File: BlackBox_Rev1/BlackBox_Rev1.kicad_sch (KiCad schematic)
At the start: 17 parts, among them J1 RJ45_LED_Shielded, J2 Molex_uF_SV_06, J3 Conn_02x08_Counter_Clockwise, SW1 SW_Push, SW2 SW_Push, U1 Teensy4.1_DEV-16771, U2 TSR1-2433

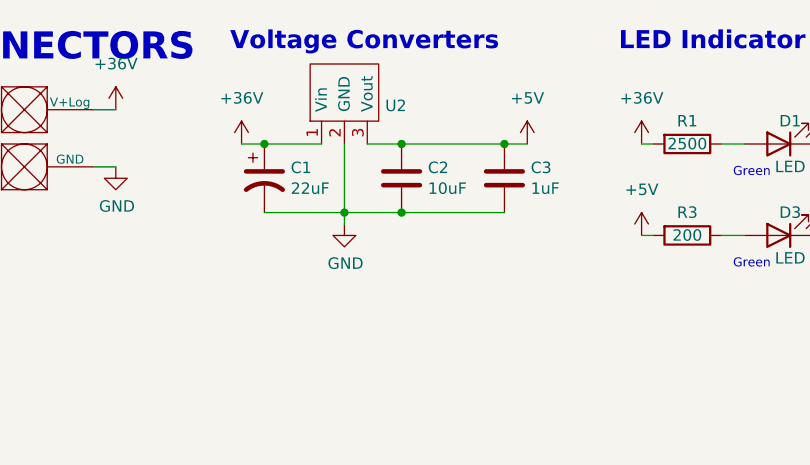
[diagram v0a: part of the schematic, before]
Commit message: change connector direction
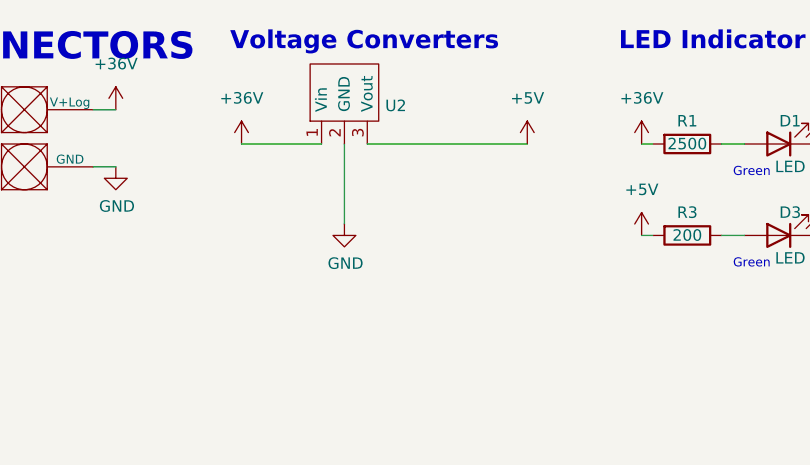
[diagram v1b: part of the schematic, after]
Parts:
- removed C1: 22uF, Capacitor_THT:CP_Radial_D5.0mm_P2.00mm, symbol BMS_2022_Rev1-rescue:CP1-Device
- removed C2: 10uF, Capacitor_SMD:C_0603_1608Metric_Pad1.08x0.95mm_HandSolder, symbol Device:C
- removed C3: 1uF, Capacitor_SMD:C_0603_1608Metric_Pad1.08x0.95mm_HandSolder, symbol Device:C
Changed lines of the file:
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@@
   (junction (at 104.14 177.8) (diameter 0) (color 0 0 0 0)
   )
-  (junction (at 67.31 34.29) (diameter 0) (color 0 0 0 0)
-  )
-  (junction (at 85.09 26.67) (diameter 0) (color 0 0 0 0)
-  )
-  (junction (at 58.42 26.67) (diameter 0) (color 0 0 0 0)
-  )
   (junction (at 66.04 189.23) (diameter 0) (color 0 0 0 0)
   )
   (junction (at 111.76 177.8) (diameter 0) (color 0 0 0 0)
-  )
-  (junction (at 73.66 34.29) (diameter 0) (color 0 0 0 0)
-  )
-  (junction (at 73.66 26.67) (diameter 0) (color 0 0 0 0)
   )
   (junction (at 104.14 166.37) (diameter 0) (color 0 0 0 0)
@@
     (stroke (width 0) (type default) (color 0 0 0 0))
   )
-  (wire (pts (xy 67.31 34.29) (xy 67.31 35.56))
-    (stroke (width 0) (type default) (color 0 0 0 0))
-  )
-  (wire (pts (xy 55.88 26.67) (xy 58.42 26.67))
-    (stroke (width 0) (type default) (color 0 0 0 0))
-  )
-  (wire (pts (xy 67.31 34.29) (xy 73.66 34.29))
+  (wire (pts (xy 67.31 26.67) (xy 67.31 35.56))
     (stroke (width 0) (type default) (color 0 0 0 0))
   )
@@
     (stroke (width 0) (type default) (color 0 0 0 0))
   )
-  (wire (pts (xy 85.09 26.67) (xy 87.63 26.67))
+  (wire (pts (xy 69.85 26.67) (xy 87.63 26.67))
     (stroke (width 0) (type default) (color 0 0 0 0))
   )
@@
     (stroke (width 0) (type default) (color 0 0 0 0))
   )
-  (wire (pts (xy 73.66 26.67) (xy 85.09 26.67))
-    (stroke (width 0) (type default) (color 0 0 0 0))
-  )
   (wire (pts (xy 156.21 152.4) (xy 158.75 152.4))
     (stroke (width 0) (type default) (color 0 0 0 0))
@@
     (stroke (width 0) (type default) (color 0 0 0 0))
   )
-  (wire (pts (xy 58.42 34.29) (xy 67.31 34.29))
-    (stroke (width 0) (type default) (color 0 0 0 0))
-  )
   (wire (pts (xy 118.11 137.16) (xy 118.11 180.34))
     (stroke (width 0) (type default) (color 0 0 0 0))
@@
     (stroke (width 0) (type default) (color 0 0 0 0))
   )
-  (wire (pts (xy 73.66 34.29) (xy 85.09 34.29))
-    (stroke (width 0) (type default) (color 0 0 0 0))
-  )
   (wire (pts (xy 104.14 160.02) (xy 104.14 166.37))
     (stroke (width 0) (type default) (color 0 0 0 0))
@@
     (stroke (width 0) (type default) (color 0 0 0 0))
   )
-  (wire (pts (xy 58.42 26.67) (xy 64.77 26.67))
+  (wire (pts (xy 55.88 26.67) (xy 64.77 26.67))
     (stroke (width 0) (type default) (color 0 0 0 0))
   )
@@
     (stroke (width 0) (type default) (color 0 0 0 0))
   )
-  (wire (pts (xy 67.31 26.67) (xy 67.31 34.29))
-    (stroke (width 0) (type default) (color 0 0 0 0))
-  )
   (wire (pts (xy 171.45 152.4) (xy 173.99 152.4))
-    (stroke (width 0) (type default) (color 0 0 0 0))
-  )
-  (wire (pts (xy 69.85 26.67) (xy 73.66 26.67))
     (stroke (width 0) (type default) (color 0 0 0 0))
   )
@@
     (pin "1")
   )
-  (symbol (lib_id "Device:C") (at 73.66 30.48 0) (unit 1)
-    (in_bom yes) (on_board yes)
-    (property "Reference" "C2" (id 0) (at 76.581 29.3116 0)
-      (effects (font (size 1.27 1.27)) (justify left))
-    )
-    (property "Value" "10uF" (id 1) (at 76.581 31.623 0)
-      (effects (font (size 1.27 1.27)) (justify left))
-    )
-    (property "Footprint" "Capacitor_SMD:C_0603_1608Metric_Pad1.08x0.95mm_HandSolder" (id 2) (at 74.6252 34.29 0)
-      (effects (font (size 1.27 1.27)) hide)
-    )
-    (property "Datasheet" "~" (id 3) (at 73.66 30.48 0)
-      (effects (font (size 1.27 1.27)) hide)
-    )
-    (pin "1")
-    (pin "2")
-  )
   (symbol (lib_id "power:+5V") (at 87.63 26.67 0) (unit 1)
     (in_bom yes) (on_board yes) (fields_autoplaced)
@@
     (pin "SH")
   )
-  (symbol (lib_id "BMS_2022_Rev1-rescue:CP1-Device") (at 58.42 30.48 0) (unit 1)
-    (in_bom yes) (on_board yes)
-    (property "Reference" "C1" (id 0) (at 61.341 29.3116 0)
-      (effects (font (size 1.27 1.27)) (justify left))
-    )
-    (property "Value" "22uF" (id 1) (at 61.341 31.623 0)
-      (effects (font (size 1.27 1.27)) (justify left))
-    )
-    (property "Footprint" "Capacitor_THT:CP_Radial_D5.0mm_P2.00mm" (id 2) (at 58.42 30.48 0)
-      (effects (font (size 1.27 1.27)) hide)
-    )
-    (property "Datasheet" "~" (id 3) (at 58.42 30.48 0)
-      (effects (font (size 1.27 1.27)) hide)
-    )
-    (pin "1")
-    (pin "2")
-  )
   (symbol (lib_id "power:GND") (at 87.63 152.4 0) (unit 1)
     (in_bom yes) (on_board yes)
@@
     (pin "1")
   )
-  (symbol (lib_id "Device:C") (at 85.09 30.48 0) (unit 1)
-    (in_bom yes) (on_board yes)
-    (property "Reference" "C3" (id 0) (at 88.011 29.3116 0)
-      (effects (font (size 1.27 1.27)) (justify left))
-    )
-    (property "Value" "1uF" (id 1) (at 88.011 31.623 0)
-      (effects (font (size 1.27 1.27)) (justify left))
-    )
-    (property "Footprint" "Capacitor_SMD:C_0603_1608Metric_Pad1.08x0.95mm_HandSolder" (id 2) (at 86.0552 34.29 0)
-      (effects (font (size 1.27 1.27)) hide)
-    )
-    (property "Datasheet" "~" (id 3) (at 85.09 30.48 0)
-      (effects (font (size 1.27 1.27)) hide)
-    )
-    (pin "1")
-    (pin "2")
-  )
   (symbol (lib_id "power:GND") (at 121.92 26.67 0) (unit 1)
     (in_bom yes) (on_board yes)
@@
       (reference "#PWR0106") (unit 1) (value "GND") (footprint "")
     )
-    (path "/c66825b9-5143-4c83-90ee-8bd89d91f6cd"
-      (reference "C1") (unit 1) (value "22uF") (footprint "Capacitor_THT:CP_Radial_D5.0mm_P2.00mm")
-    )
-    (path "/b0f91748-63da-4b62-9113-8f4f59d6fbad"
-      (reference "C2") (unit 1) (value "10uF") (footprint "Capacitor_SMD:C_0603_1608Metric_Pad1.08x0.95mm_HandSolder")
-    )
-    (path "/f1873180-95f5-41e2-bc79-a07462325bb2"
-      (reference "C3") (unit 1) (value "1uF") (footprint "Capacitor_SMD:C_0603_1608Metric_Pad1.08x0.95mm_HandSolder")
-    )
     (path "/9d9ed59e-cc22-4a1e-998b-26ca9d73f23c"

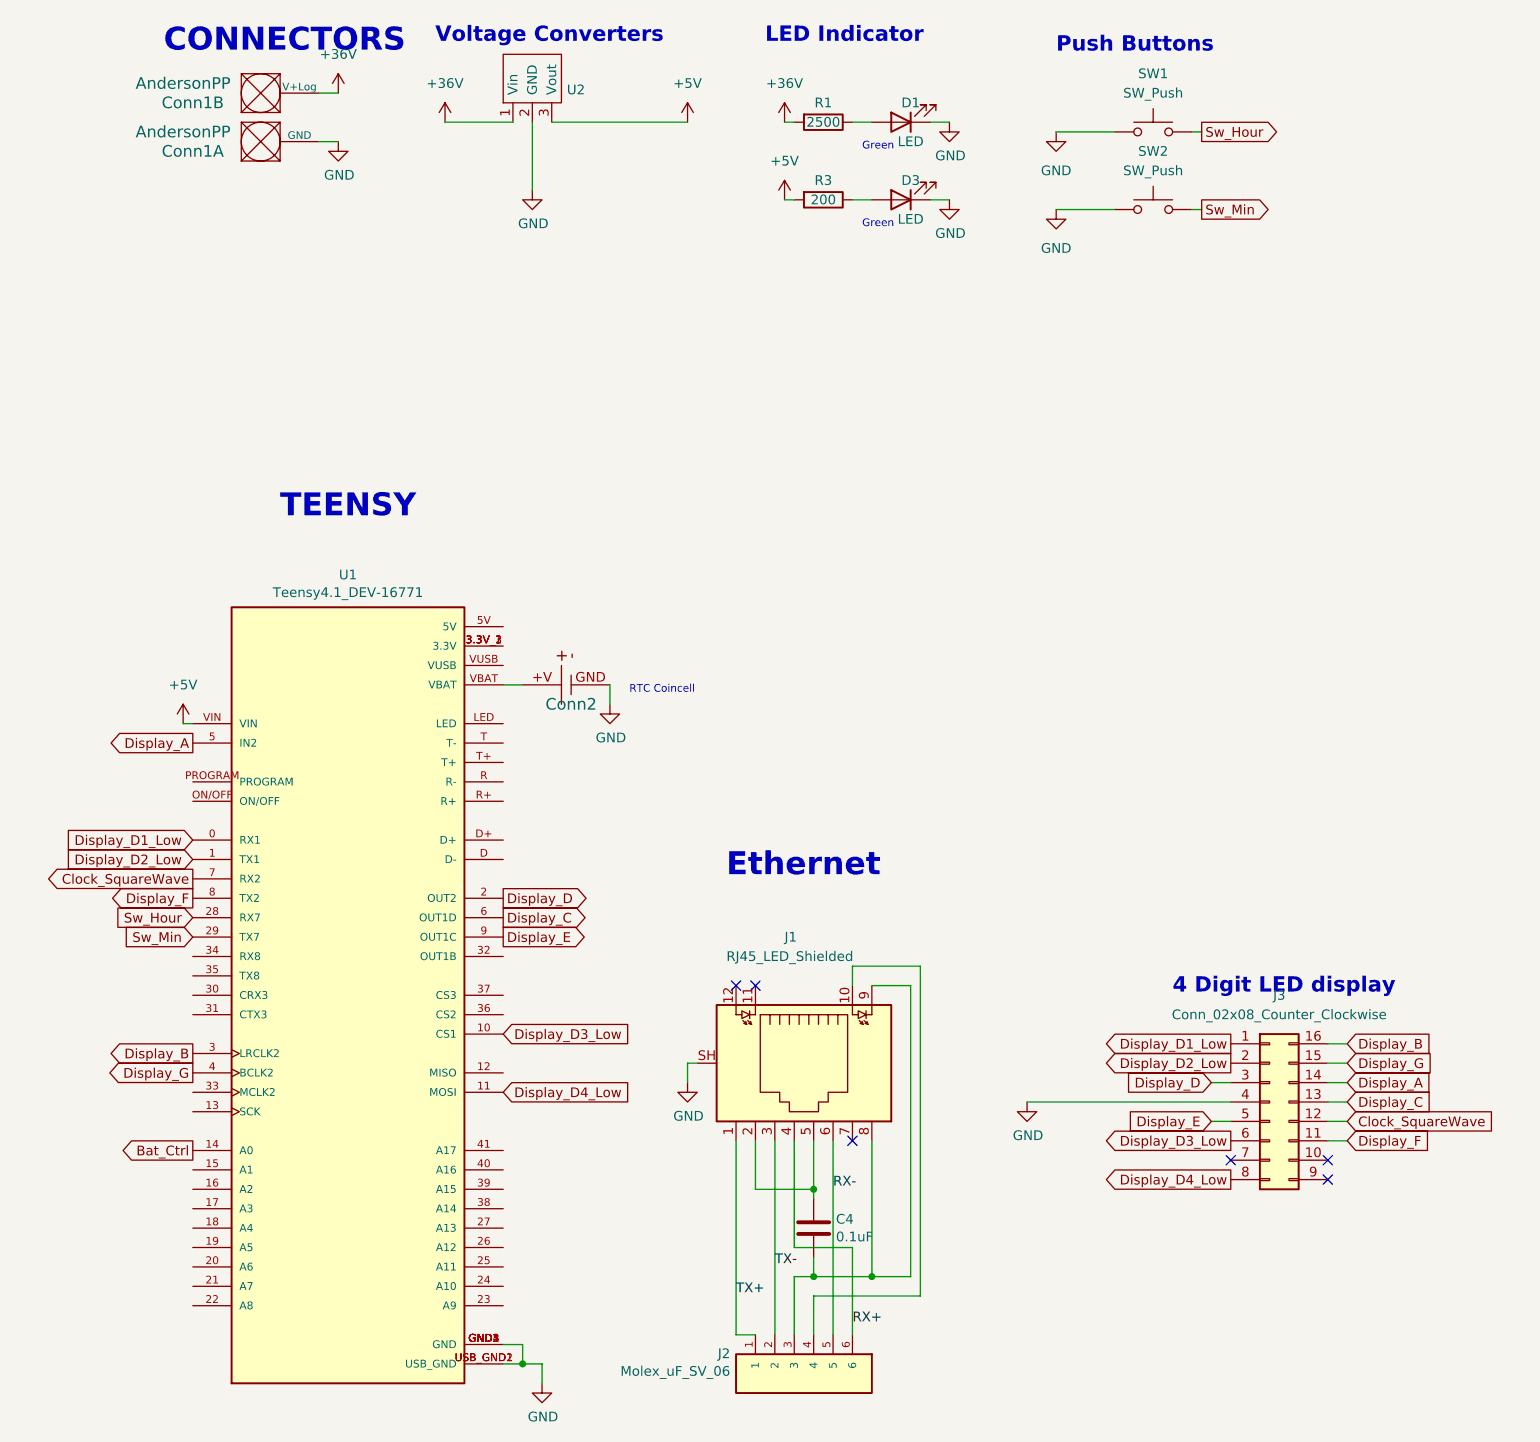
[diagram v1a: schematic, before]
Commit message: added resistors to protect teensy
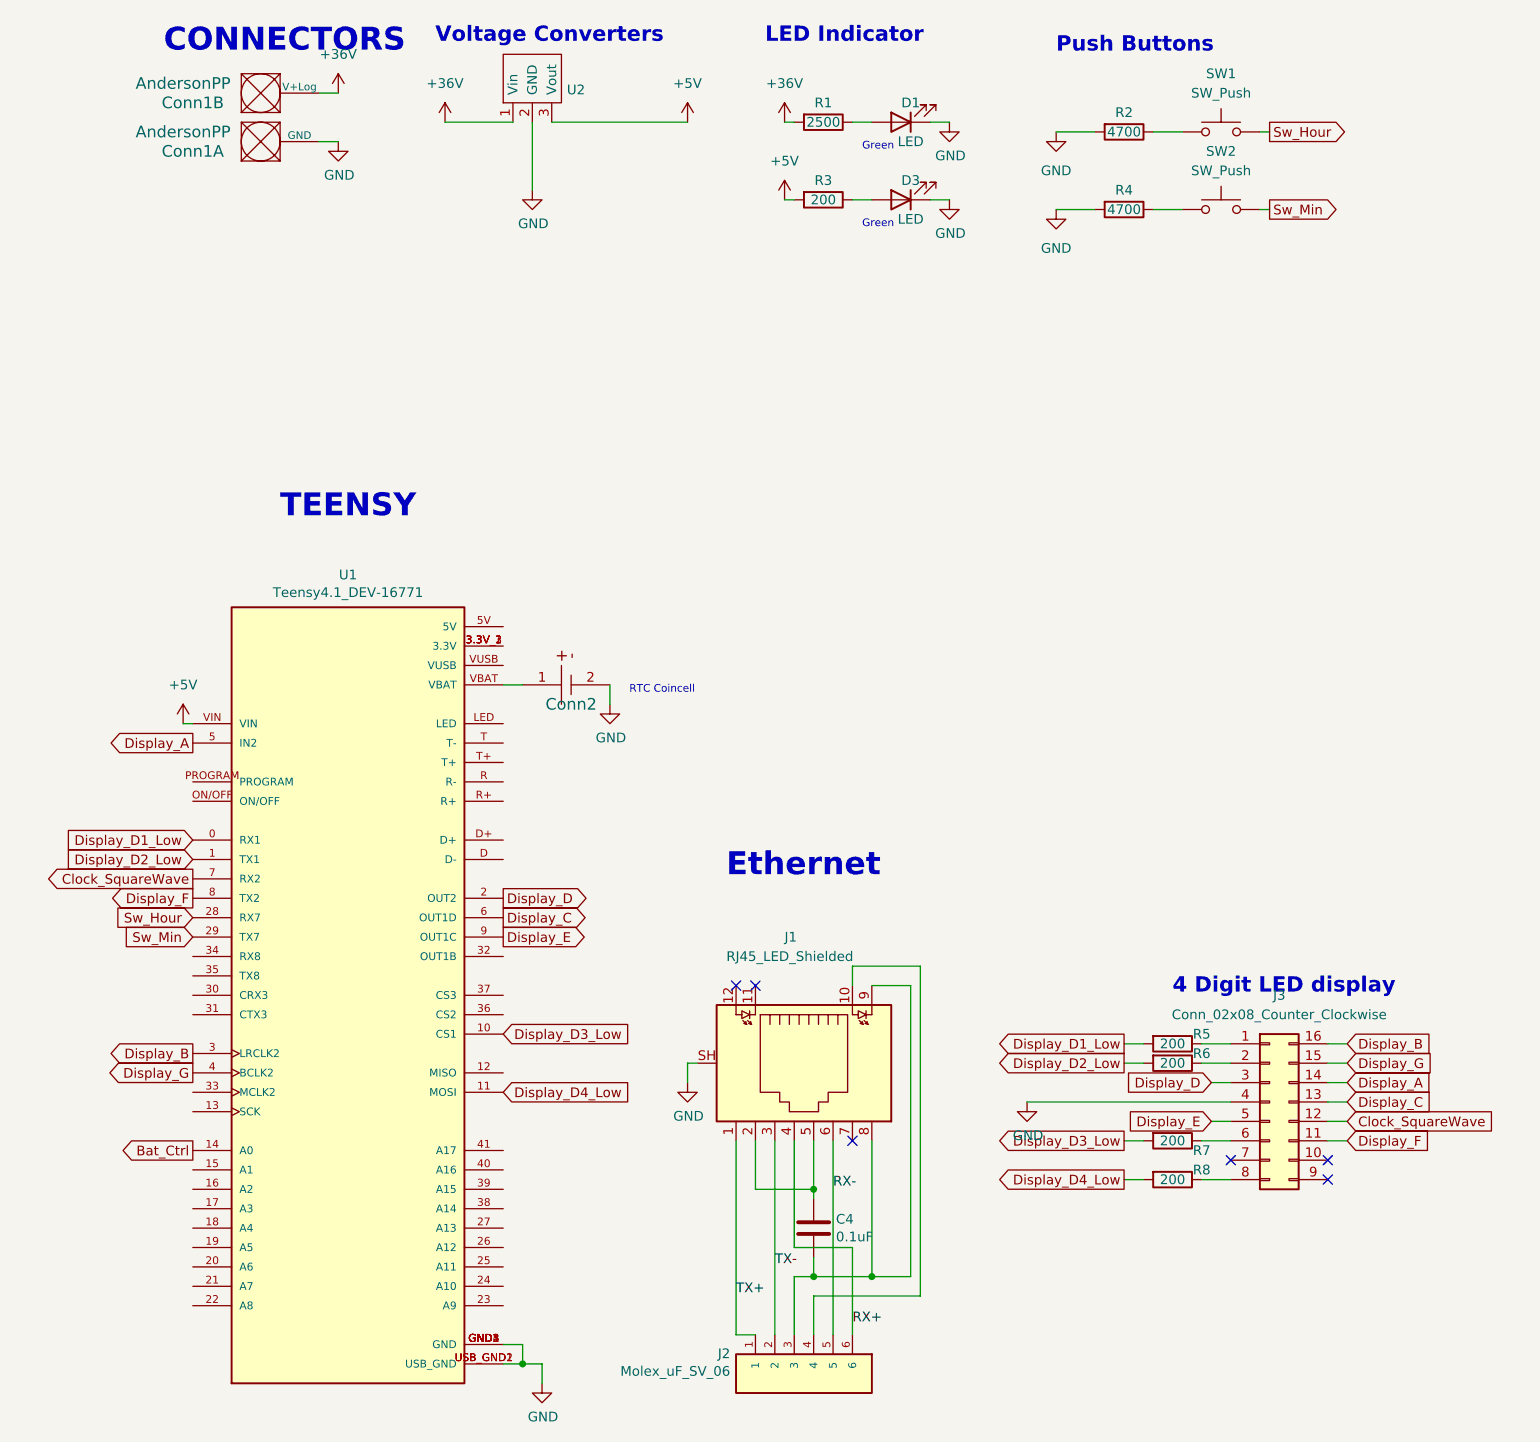
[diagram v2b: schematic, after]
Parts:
- added R2, R4: 4700, Resistor_SMD:R_0603_1608Metric_Pad0.98x0.95mm_HandSolder, symbol Device:R
- added R5, R6, R7, R8: 200, Resistor_SMD:R_0603_1608Metric_Pad0.98x0.95mm_HandSolder, symbol Device:R
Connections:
- net Display_D1_Low: now also R5.2; no longer J3.1 (Pin_1)
- net Display_D2_Low: now also R6.2; no longer J3.2 (Pin_2)
- net Display_D3_Low: now also R7.2; no longer J3.6 (Pin_6)
- net Display_D4_Low: now also R8.2; no longer J3.8 (Pin_8)
- net GND: now also Conn2.2, R2.2, R4.2; no longer Conn2.GND, SW1.1, SW2.1
- net at U1.VBAT: now also Conn2.1; no longer Conn2.+V
- new net: R4.1, SW2.1
- new net: J3.8 (Pin_8), R8.1
- new net: J3.1 (Pin_1), R5.1
- new net: J3.2 (Pin_2), R6.1
- new net: J3.6 (Pin_6), R7.1
- new net: R2.1, SW1.1
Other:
- moved on the sheet: SW1, SW2

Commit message: switch teensy and pushbutton to 3v3
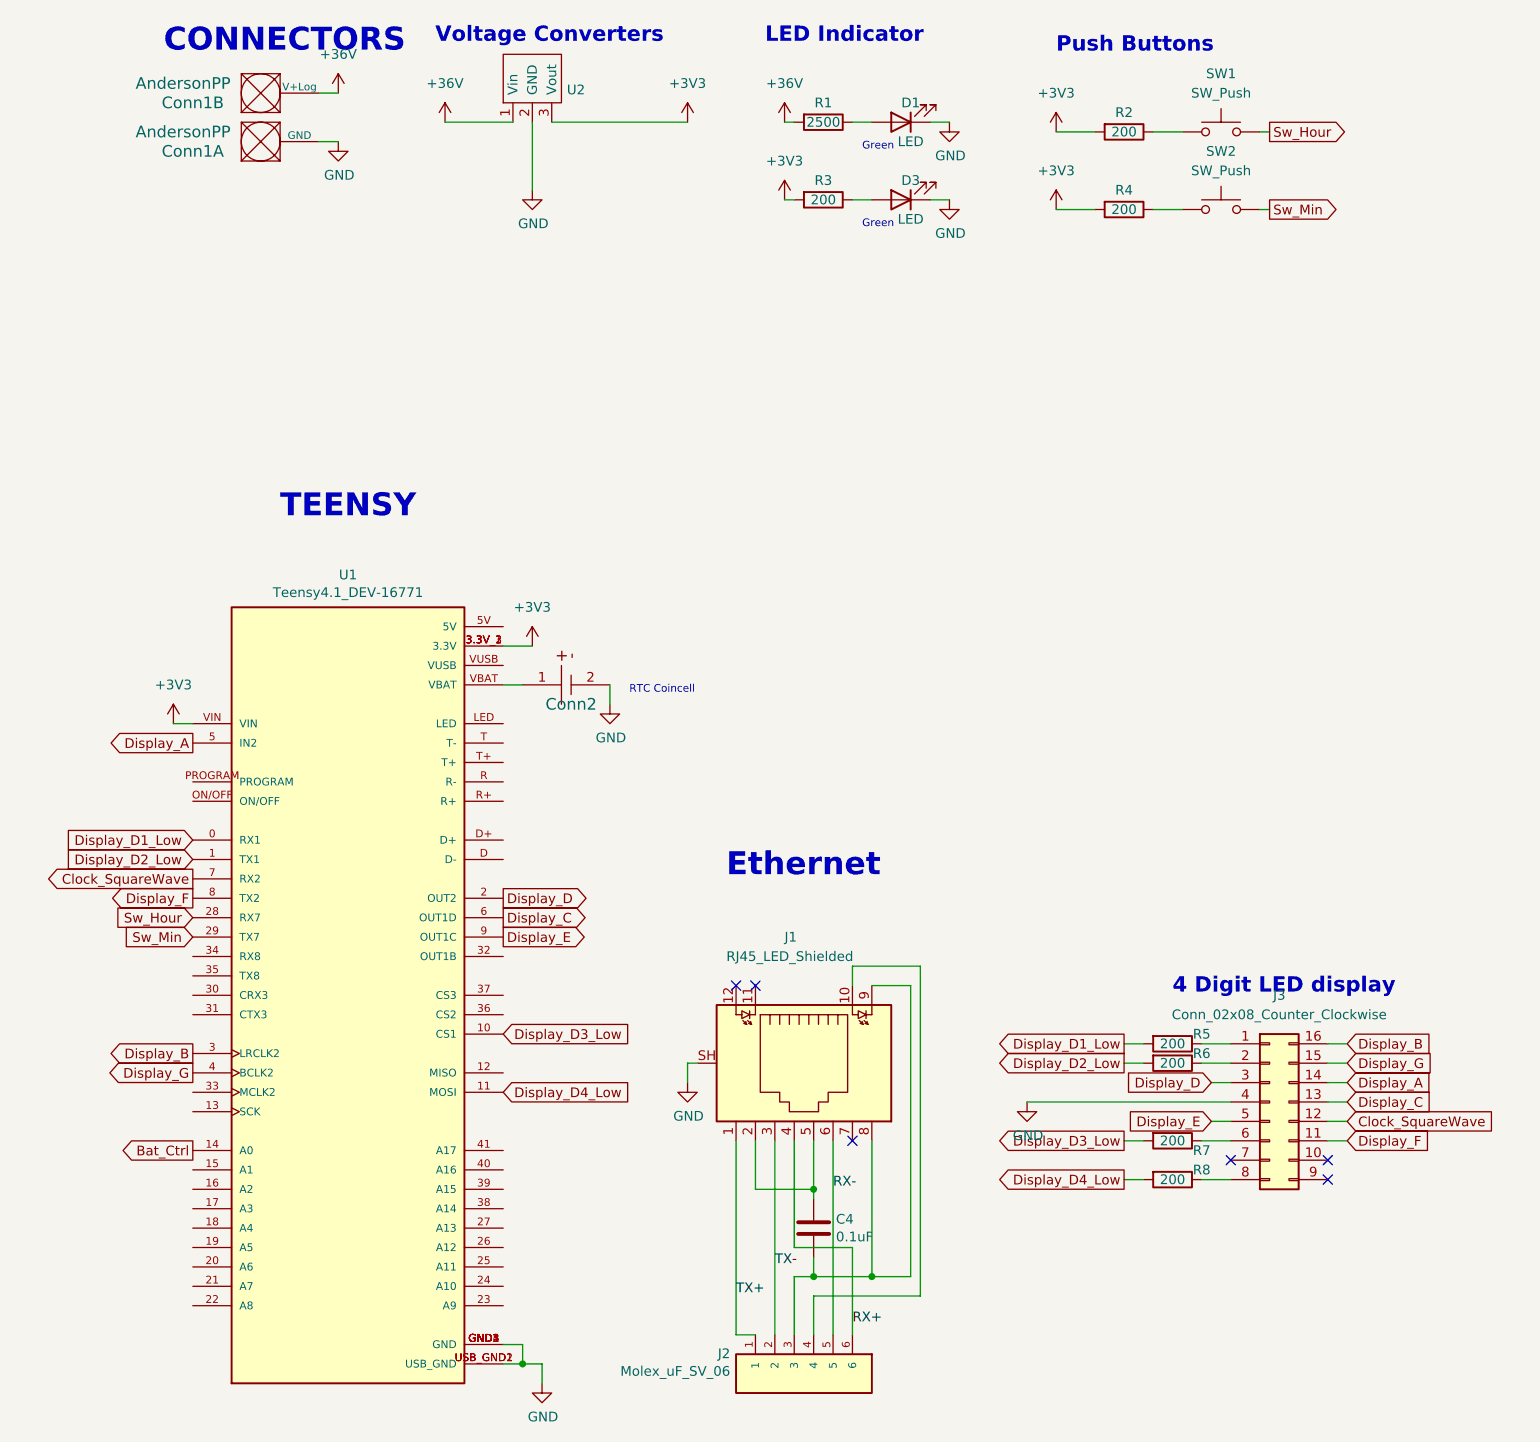
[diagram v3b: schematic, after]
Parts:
- R2, R4: value 4700 -> 200
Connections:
- net +5V is gone; now on net +3V3: R3.2, U1.VIN, U2.3 (Vout)
- net GND: no longer R2.2, R4.2
- net +3V3: now reaches U1.3.3V_1 (3.3V), U1.3.3V_2 (3.3V), U1.3.3V_3 (3.3V)
- net +3V3: now also R2.2, R4.2
